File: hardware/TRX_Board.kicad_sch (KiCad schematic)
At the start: 60 parts, among them J1 Conn_02x08_Odd_Even, J2 SMA, J3 Conn_01x03, J4 Conn_01x03, Q1 BSN20, Q2 BSN20, Q3 BSN20, U1 AP1117-33, U2 LM386, U3 DRA818U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

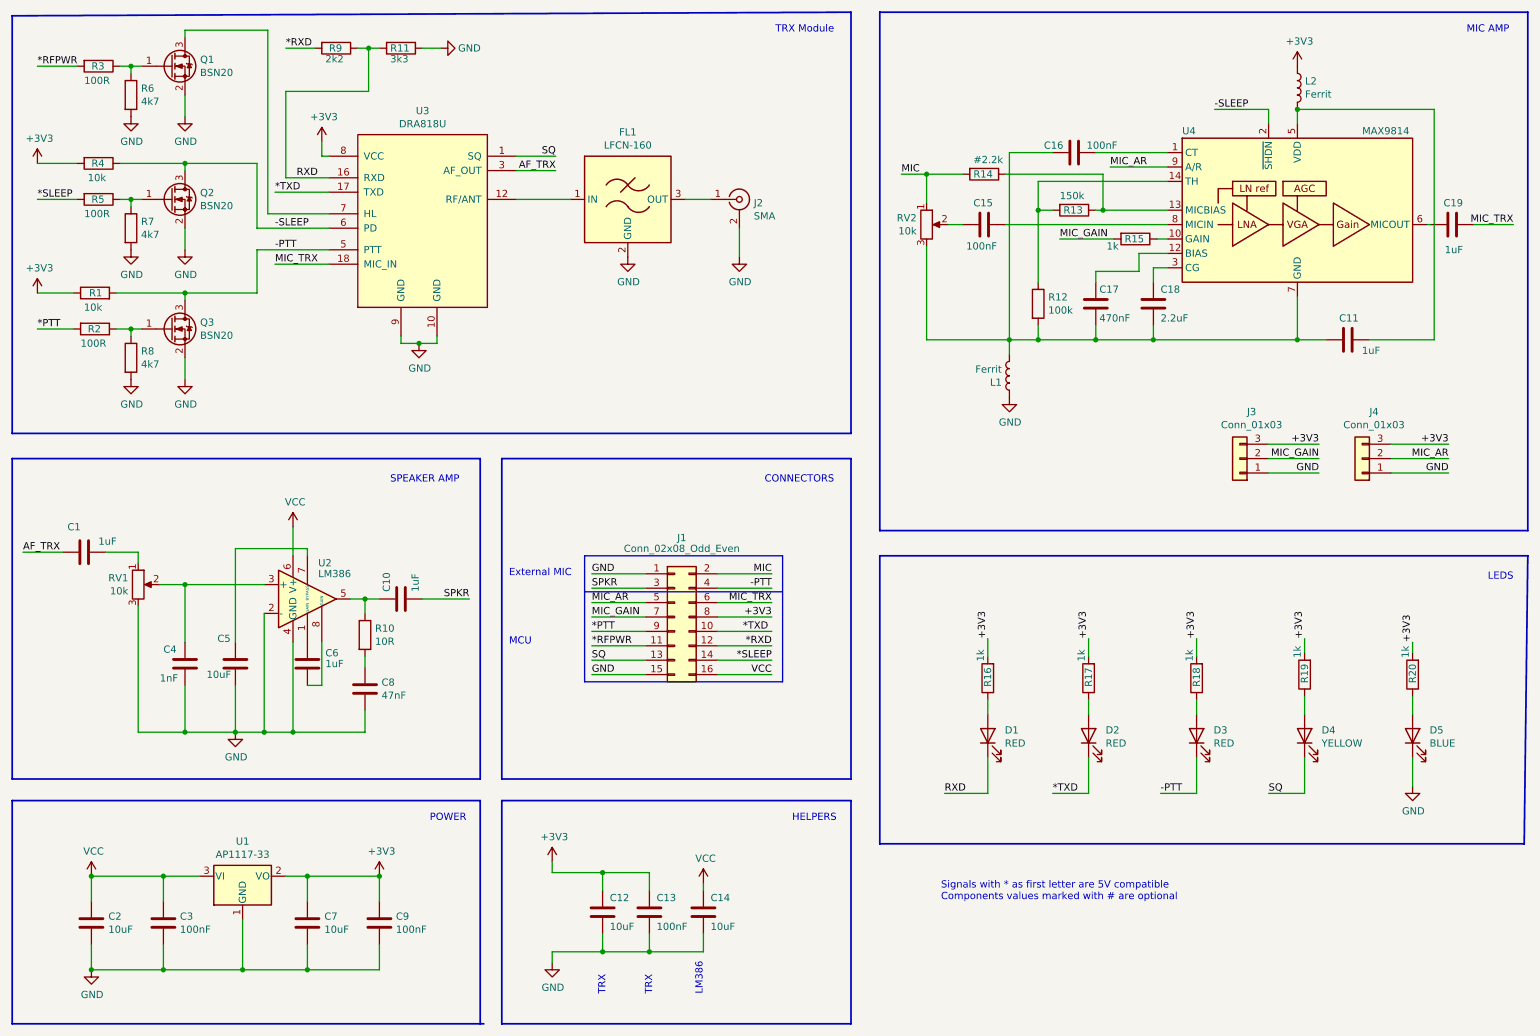
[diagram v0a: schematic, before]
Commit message: updated schematic for better mic support / added documents
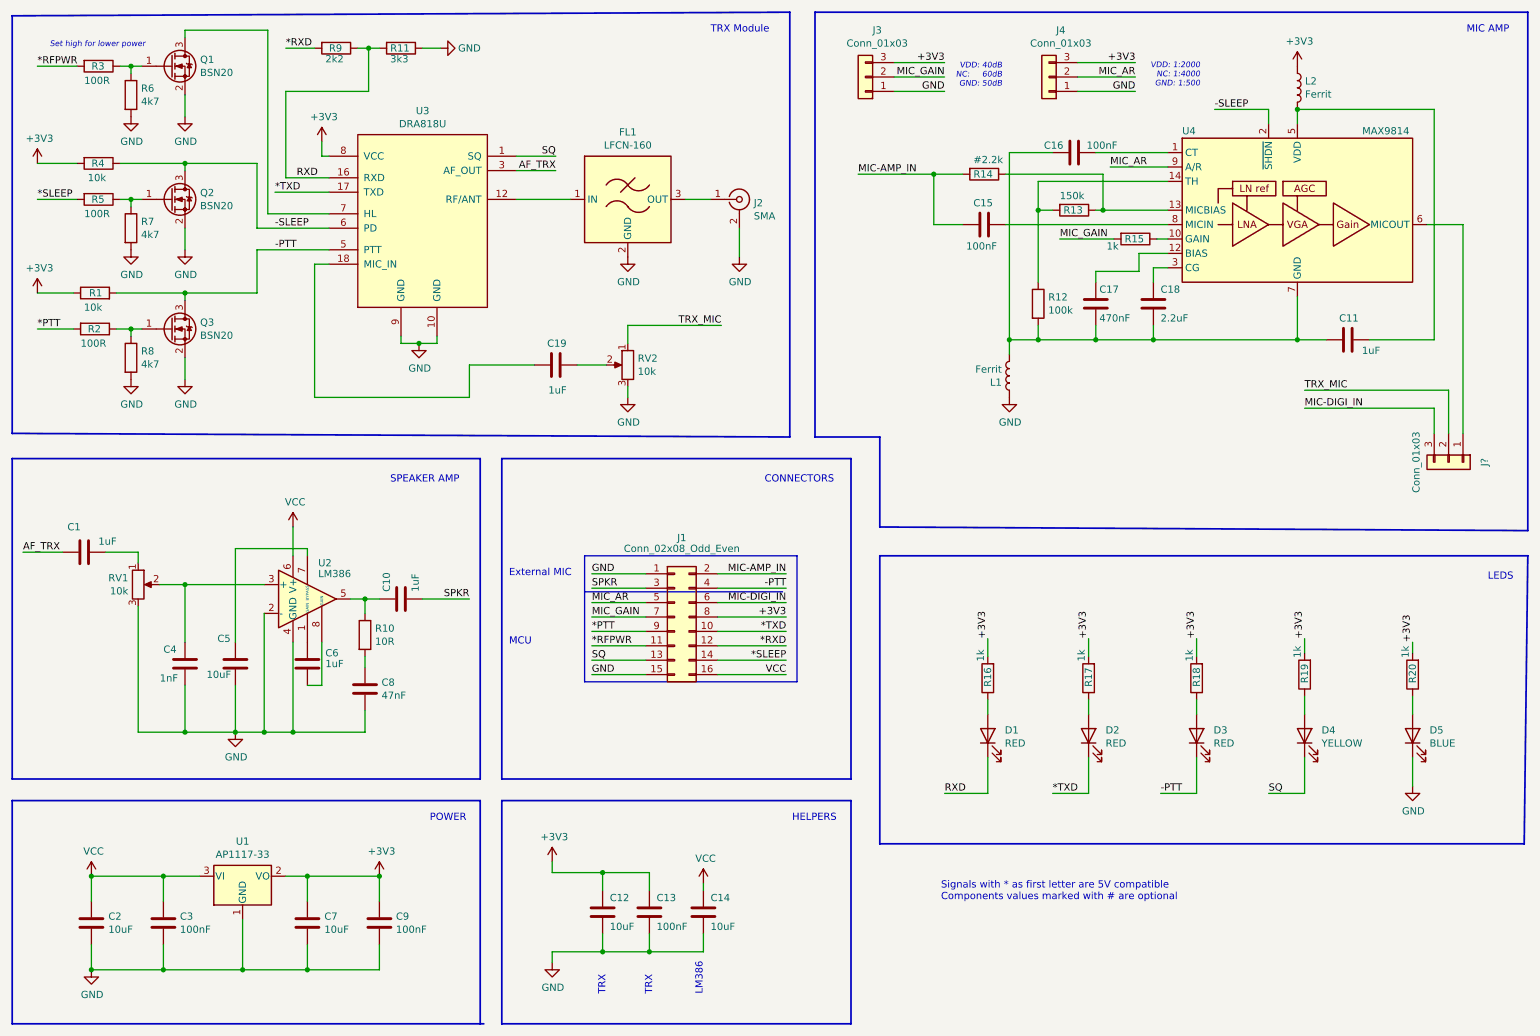
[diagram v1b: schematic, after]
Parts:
- added J?: Conn_01x03, Connector_PinHeader_2.54mm:PinHeader_1x03_P2.54mm_Vertical, symbol Connector_Generic:Conn_01x03
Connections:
- net GND: now also RV2.3
- net at C11.1, C16.1, C17.2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: no longer RV2.3
- net at C19.1: now also U3.18 (MIC_IN); no longer U4.6 (MICOUT)
- net at RV2.2: now also C19.2; no longer C15.2
- net MIC renamed MIC-AMP_IN
- net MIC-AMP_IN: now also C15.2; no longer RV2.1
- removed net MIC_TRX: C19.2, J1.6 (Pin_6), U3.18 (MIC_IN)
- new net: J?.1 (Pin_1), U4.6 (MICOUT)
- new net MIC-DIGI_IN: J1.6 (Pin_6), J?.3 (Pin_3)
- new net TRX_MIC: J?.2 (Pin_2), RV2.1
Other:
- note added: "Set high for lower power"
- note added: "VDD: 1:2000 NC: 1:4000 GND: 1:500"
- note added: "VDD: 40dB NC: 60dB GND: 50dB"
- moved on the sheet: C19, J3, J4, RV2

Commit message: Optimized MIC path for electret and digital sources / added separated dirs for Gerbers
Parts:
- J5: renamed from J?; footprint Connector_PinHeader_2.54mm:PinHeader_1x03_P2.54mm_Vertical -> Jumper:SolderJumper-3_P2.0mm_Open_TrianglePad1.0x1.5mm_NumberLabels
- Q1, Q2, Q3: LCSC C10487 -> C20917
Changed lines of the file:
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@@
       (effects (font (size 1.27 1.27) italic) (justify left) hide)
     )
-    (property "Datasheet" "https://datasheet.lcsc.com/lcsc/1808272021_Vishay-Intertech-SI2301CDS-T1-GE3_C10487.pdf" (id 3) (at 42.545 70.485 0)
+    (property "Datasheet" "https://datasheet.lcsc.com/lcsc/1811081213_Alpha---Omega-Semicon-AO3400A_C20917.pdf" (id 3) (at 42.545 70.485 0)
       (effects (font (size 1.27 1.27)) (justify left) hide)
     )
-    (property "LCSC" "C10487" (id 4) (at 42.545 70.485 0)
+    (property "LCSC" "C20917" (id 4) (at 42.545 70.485 0)
       (effects (font (size 1.27 1.27)) hide)
     )
@@
       (effects (font (size 1.27 1.27) italic) (justify left) hide)
     )
-    (property "Datasheet" "https://datasheet.lcsc.com/lcsc/1808272021_Vishay-Intertech-SI2301CDS-T1-GE3_C10487.pdf" (id 3) (at 42.545 47.625 0)
+    (property "Datasheet" "https://datasheet.lcsc.com/lcsc/1811081213_Alpha---Omega-Semicon-AO3400A_C20917.pdf" (id 3) (at 42.545 47.625 0)
       (effects (font (size 1.27 1.27)) (justify left) hide)
     )
-    (property "LCSC" "C10487" (id 4) (at 42.545 47.625 0)
+    (property "LCSC" "C20917" (id 4) (at 42.545 47.625 0)
       (effects (font (size 1.27 1.27)) hide)
     )
@@
       (effects (font (size 1.27 1.27) italic) (justify left) hide)
     )
-    (property "Datasheet" "https://datasheet.lcsc.com/lcsc/1808272021_Vishay-Intertech-SI2301CDS-T1-GE3_C10487.pdf" (id 3) (at 42.545 24.13 0)
+    (property "Datasheet" "https://datasheet.lcsc.com/lcsc/1811081213_Alpha---Omega-Semicon-AO3400A_C20917.pdf" (id 3) (at 42.545 24.13 0)
       (effects (font (size 1.27 1.27)) (justify left) hide)
     )
-    (property "LCSC" "C10487" (id 4) (at 42.545 24.13 0)
+    (property "LCSC" "C20917" (id 4) (at 42.545 24.13 0)
       (effects (font (size 1.27 1.27)) hide)
     )
@@
   (symbol (lib_id "power:GND") (at 123.19 82.55 0) (unit 1)
     (in_bom yes) (on_board yes)
-    (property "Reference" "#PWR?" (id 0) (at 123.19 88.9 0)
+    (property "Reference" "#PWR02" (id 0) (at 123.19 88.9 0)
       (effects (font (size 1.27 1.27)) hide)
     )
@@
   (symbol (lib_id "Connector_Generic:Conn_01x03") (at 267.97 93.98 270) (unit 1)
     (in_bom yes) (on_board yes)
-    (property "Reference" "J?" (id 0) (at 274.32 93.98 0))
+    (property "Reference" "J5" (id 0) (at 274.32 93.98 0))
     (property "Value" "Conn_01x03" (id 1) (at 262.255 93.98 0))
-    (property "Footprint" "Connector_PinHeader_2.54mm:PinHeader_1x03_P2.54mm_Vertical" (id 2) (at 267.97 93.98 0)
+    (property "Footprint" "Jumper:SolderJumper-3_P2.0mm_Open_TrianglePad1.0x1.5mm_NumberLabels" (id 2) (at 267.97 93.98 0)
       (effects (font (size 1.27 1.27)) hide)
     )
@@
       (reference "#PWR01") (unit 1) (value "GND") (footprint "")
     )
+    (path "/8d15e4a3-4d3b-4b83-8857-11d9a1b60429"
+      (reference "#PWR02") (unit 1) (value "GND") (footprint "")
+    )
     (path "/00000000-0000-0000-0000-000061a7cf8b"
       (reference "#PWR0101") (unit 1) (value "GND") (footprint "")
@@
       (reference "#PWR0123") (unit 1) (value "+3V3") (footprint "")
     )
-    (path "/8d15e4a3-4d3b-4b83-8857-11d9a1b60429"
-      (reference "#PWR?") (unit 1) (value "GND") (footprint "")
-    )
     (path "/00000000-0000-0000-0000-000061adb17e"
       (reference "C1") (unit 1) (value "1uF") (footprint "Capacitor_SMD:C_0805_2012Metric")
@@
     )
     (path "/a72b9da8-589b-45ae-a2e0-4bd5e50dc3c5"
-      (reference "J?") (unit 1) (value "Conn_01x03") (footprint "Connector_PinHeader_2.54mm:PinHeader_1x03_P2.54mm_Vertical")
+      (reference "J5") (unit 1) (value "Conn_01x03") (footprint "Jumper:SolderJumper-3_P2.0mm_Open_TrianglePad1.0x1.5mm_NumberLabels")
     )
     (path "/00000000-0000-0000-0000-000061bd53ee"
